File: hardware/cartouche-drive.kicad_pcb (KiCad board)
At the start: 4 copper layers, 36 x 46 mm, 71 parts, among them J1 USB-C 105450-0101, J2 M.2 key M (2230), U1 JMS583, U2 TPS82130, U3 ZD25WQ16, Y1 25MHz 12pF

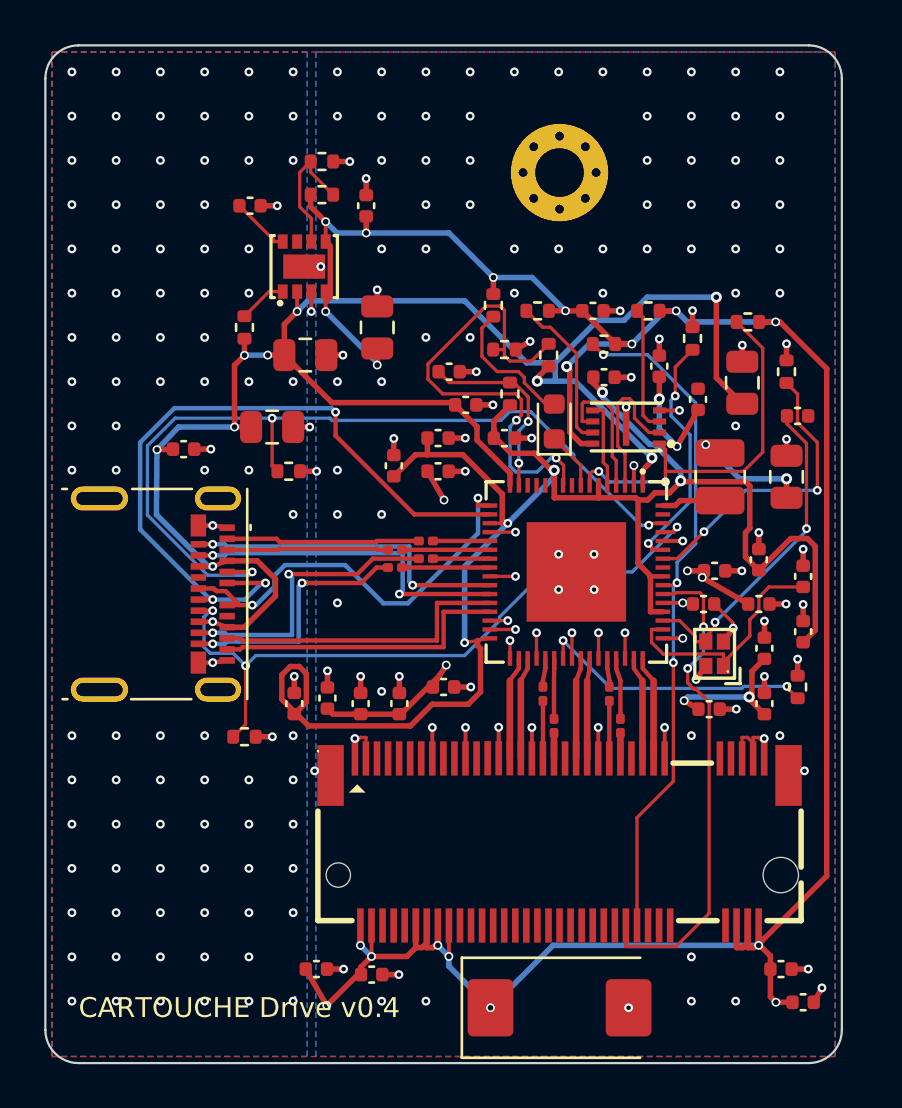
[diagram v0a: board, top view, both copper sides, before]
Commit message: USB-C face at the board edge (outline moved 0.675 mm)
The Molex 105450 footprint marks the PCB edge 4.325 mm in front of its origin;
the board stuck out 0.675 mm in front of the receptacle, so a plug's overmould
would hit it. tools/usb_edge.py moves the whole outline and the outer pour edges
right by 0.675 mm (board still 36 x 46 mm); one corner stitching via removed.
DRC: 0 unconnected. Gerbers, drill, CPL, renders re-exported.

Co-Authored-By: Claude Opus 5.5 <noreply@anthropic.com>
Claude-Session: https://claude.ai/code/session_01RqDGjrUG4GdEsawKGChjmB
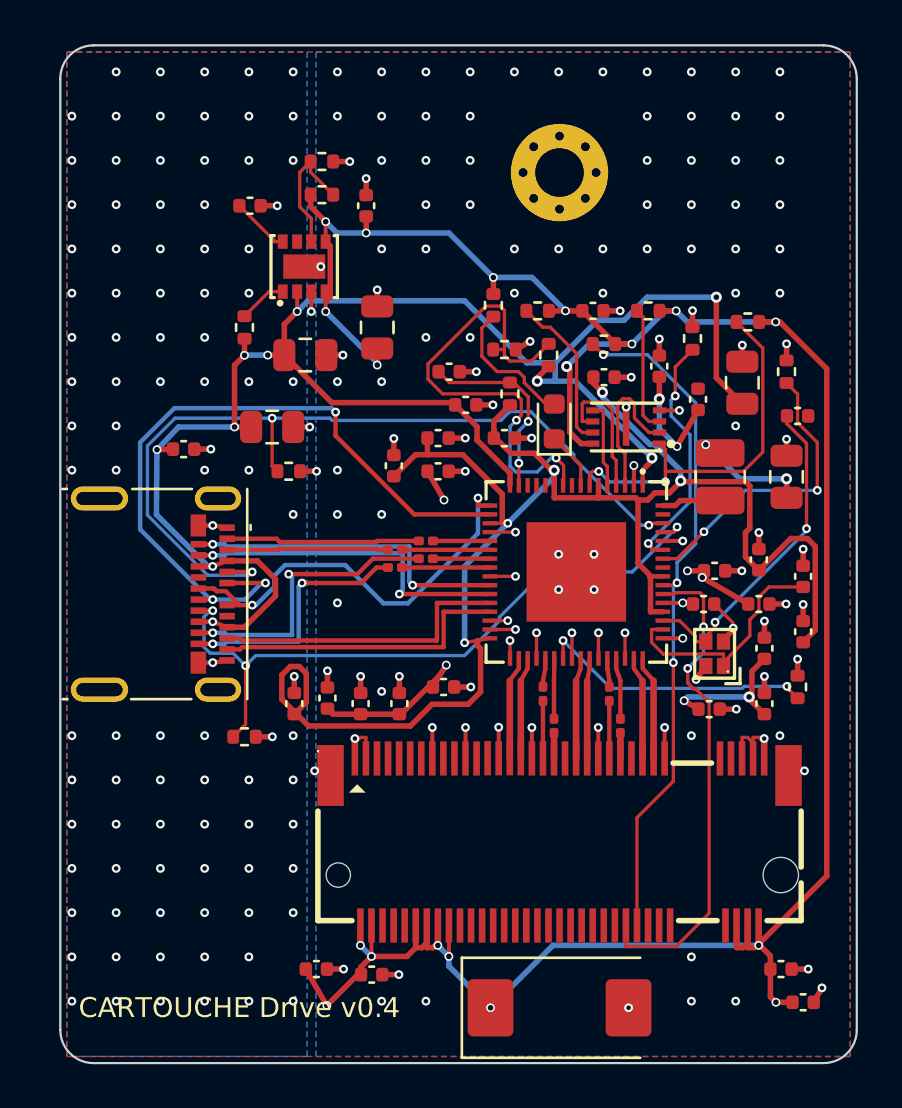
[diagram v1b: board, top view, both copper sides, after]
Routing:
- net /GND: vias 216 -> 215
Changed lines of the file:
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@@
 	)
 	(gr_line
-		(start 1.5 0)
-		(end 34.5 0)
+		(start 2.175 0)
+		(end 35.175 0)
 		(stroke
 			(width 0.1)
@@
 	)
 	(gr_arc
-		(start 34.5 0)
-		(mid 35.56066 0.43934)
-		(end 36 1.5)
+		(start 35.175 0)
+		(mid 36.23566 0.43934)
+		(end 36.675 1.5)
 		(stroke
 			(width 0.1)
@@
 	)
 	(gr_arc
-		(start 1.5 46)
-		(mid 0.43934 45.56066)
-		(end 0 44.5)
+		(start 2.175 46)
+		(mid 1.11434 45.56066)
+		(end 0.675 44.5)
 		(stroke
 			(width 0.1)
@@
 	)
 	(gr_arc
-		(start 36 44.5)
-		(mid 35.56066 45.56066)
-		(end 34.5 46)
+		(start 36.675 44.5)
+		(mid 36.23566 45.56066)
+		(end 35.175 46)
 		(stroke
 			(width 0.1)
@@
 	)
 	(gr_line
-		(start 36 1.5)
-		(end 36 44.5)
+		(start 36.675 1.5)
+		(end 36.675 44.5)
 		(stroke
 			(width 0.1)
@@
 	)
 	(gr_arc
-		(start 0 1.5)
-		(mid 0.43934 0.43934)
-		(end 1.5 0)
+		(start 0.675 1.5)
+		(mid 1.11434 0.43934)
+		(end 2.175 0)
 		(stroke
 			(width 0.1)
@@
 	)
 	(gr_line
-		(start 0 44.5)
-		(end 0 1.5)
+		(start 0.675 44.5)
+		(end 0.675 1.5)
 		(stroke
 			(width 0.1)
@@
 	)
 	(gr_line
-		(start 34.5 46)
-		(end 1.5 46)
+		(start 35.175 46)
+		(end 2.175 46)
 		(stroke
 			(width 0.1)
@@
 	)
 	(via
-		(at 1.2 1.2)
-		(size 0.4)
-		(drill 0.2)
-		(layers "F.Cu" "B.Cu")
-		(net 4)
-	)
-	(via
 		(at 3.2 1.2)
 		(size 0.4)
@@
 		(polygon
 			(pts
-				(xy 0.3 0.3) (xy 35.7 0.3) (xy 35.7 45.7) (xy 0.3 45.7)
+				(xy 0.975 0.3) (xy 36.375 0.3) (xy 36.375 45.7) (xy 0.975 45.7)
 			)
 		)
@@
 		(polygon
 			(pts
-				(xy 0.3 0.3) (xy 11.83 0.3) (xy 11.83 45.7) (xy 0.3 45.7)
+				(xy 0.975 0.3) (xy 11.83 0.3) (xy 11.83 45.7) (xy 0.975 45.7)
 			)
 		)
@@
 		(polygon
 			(pts
-				(xy 12.229999 0.3) (xy 35.7 0.3) (xy 35.7 45.7) (xy 12.229999 45.7)
+				(xy 12.229999 0.3) (xy 36.375 0.3) (xy 36.375 45.7) (xy 12.229999 45.7)
 			)
 		)
@@
 		(polygon
 			(pts
-				(xy 0.3 0.3) (xy 35.7 0.3) (xy 35.7 45.7) (xy 0.3 45.7)
+				(xy 0.975 0.3) (xy 36.375 0.3) (xy 36.375 45.7) (xy 0.975 45.7)
 			)
 		)
@@
 		(polygon
 			(pts
-				(xy 0.3 0.3) (xy 35.7 0.3) (xy 35.7 45.7) (xy 0.3 45.7)
+				(xy 0.975 0.3) (xy 36.375 0.3) (xy 36.375 45.7) (xy 0.975 45.7)
 			)
 		)
